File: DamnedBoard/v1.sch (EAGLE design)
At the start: 17 parts, among them U1 EFM32ZG108, U2 MAX44009EDT+T21-0490D-M

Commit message: OSH Parkifying layout.
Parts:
- removed R3: 0, SparkFun-Resistors:0OHM-0603-1/10W-5%
- added JP2, JP3: JUMPER-SMT_2_NC_TRACE_NO-SILK, SparkFun-Jumpers:JUMPER-SMT_2_NC_TRACE_NO-SILK
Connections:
- removed net N$1: G1.+, R3.2
- new net +L: G1.+$1, JP2.2
- new net +R: G1.+$2, JP3.2
- net VCC: now also JP2.1, JP3.1; no longer R3.1
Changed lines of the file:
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@@
 <parts>
 <part name="TC1" library="TagConnect" deviceset="TC2050-IDC" device=""/>
-<part name="G1" library="boneyard" deviceset="LINX_BAT_HLD_001" device="" package3d_urn="urn:adsk.eagle:package:291704/2"/>
 <part name="U2" library="boneyard" deviceset="MAX44009EDT+T" device="21-0490D-M" package3d_urn="urn:adsk.eagle:package:291621/2"/>
 <part name="U1" library="boneyard" deviceset="EFM32ZG108" device=""/>
@@
 <part name="R2" library="SparkFun-Resistors" library_urn="urn:adsk.eagle:library:532" deviceset="68OHM" device="-0603-1/10W-1%" package3d_urn="urn:adsk.eagle:package:39650/1"/>
 <part name="U$1" library="boneyard" deviceset="DAMNED" device=""/>
-<part name="R3" library="SparkFun-Resistors" library_urn="urn:adsk.eagle:library:532" deviceset="0OHM" device="-0603-1/10W-5%" package3d_urn="urn:adsk.eagle:package:39650/1" value="0"/>
 <part name="C1" library="SparkFun-Capacitors" library_urn="urn:adsk.eagle:library:510" deviceset="1.0UF" device="-0603-16V-10%" package3d_urn="urn:adsk.eagle:package:37414/1" value="1.0uF"/>
 <part name="JP1" library="SparkFun-Jumpers" library_urn="urn:adsk.eagle:library:528" deviceset="JUMPER-SMT_2_NC_TRACE" device="_NO-SILK" package3d_urn="urn:adsk.eagle:package:39286/1"/>
@@
 <part name="C5" library="SparkFun-Capacitors" library_urn="urn:adsk.eagle:library:510" deviceset="0.1UF" device="-0402-16V-10%" package3d_urn="urn:adsk.eagle:package:37413/1" value="0.1uF"/>
 <part name="C6" library="SparkFun-Capacitors" library_urn="urn:adsk.eagle:library:510" deviceset="10UF" device="-0603-6.3V-20%" package3d_urn="urn:adsk.eagle:package:37414/1" value="10uF"/>
+<part name="G1" library="boneyard" deviceset="LINX_BAT_HLD_001" device="" package3d_urn="urn:adsk.eagle:package:291704/2"/>
+<part name="JP2" library="SparkFun-Jumpers" library_urn="urn:adsk.eagle:library:528" deviceset="JUMPER-SMT_2_NC_TRACE" device="_NO-SILK" package3d_urn="urn:adsk.eagle:package:39286/1"/>
+<part name="JP3" library="SparkFun-Jumpers" library_urn="urn:adsk.eagle:library:528" deviceset="JUMPER-SMT_2_NC_TRACE" device="_NO-SILK" package3d_urn="urn:adsk.eagle:package:39286/1"/>
 </parts>
 <sheets>
@@
 <instances>
 <instance part="TC1" gate="A" x="-27.94" y="50.8" rot="R180"/>
-<instance part="G1" gate="G$1" x="43.18" y="27.94"/>
 <instance part="U2" gate="A" x="86.36" y="22.86"/>
 <instance part="U1" gate="G$1" x="55.88" y="55.88"/>
@@
 </instance>
 <instance part="U$1" gate="G$1" x="48.26" y="104.14"/>
-<instance part="R3" gate="G$1" x="27.94" y="27.94"/>
 <instance part="C1" gate="G$1" x="142.24" y="63.5"/>
 <instance part="JP1" gate="G$1" x="33.02" y="58.42" smashed="yes">
@@
 <instance part="C5" gate="G$1" x="17.78" y="71.12"/>
 <instance part="C6" gate="G$1" x="5.08" y="71.12"/>
+<instance part="G1" gate="G$1" x="50.8" y="12.7"/>
+<instance part="JP2" gate="G$1" x="35.56" y="15.24" smashed="yes">
+<attribute name="NAME" x="33.02" y="17.78" size="1.778" layer="95" font="vector"/>
+</instance>
+<instance part="JP3" gate="G$1" x="35.56" y="10.16" smashed="yes">
+<attribute name="NAME" x="33.02" y="5.08" size="1.778" layer="95" font="vector"/>
+</instance>
 </instances>
 <busses>
@@
 <net name="VSS" class="0">
 <segment>
-<pinref part="G1" gate="G$1" pin="-"/>
 <pinref part="U1" gate="G$1" pin="VSS"/>
-<wire x1="53.34" y1="27.94" x2="76.2" y2="27.94" width="0.1524" layer="91"/>
-<wire x1="76.2" y1="27.94" x2="76.2" y2="43.18" width="0.1524" layer="91"/>
+<wire x1="76.2" y1="20.32" x2="76.2" y2="43.18" width="0.1524" layer="91"/>
 <pinref part="U2" gate="A" pin="GND"/>
 <wire x1="88.9" y1="20.32" x2="76.2" y2="20.32" width="0.1524" layer="91"/>
-<wire x1="76.2" y1="20.32" x2="76.2" y2="27.94" width="0.1524" layer="91"/>
-<junction x="76.2" y="27.94"/>
 <pinref part="U2" gate="A" pin="A0"/>
 <wire x1="88.9" y1="17.78" x2="76.2" y2="17.78" width="0.1524" layer="91"/>
@@
 <junction x="76.2" y="20.32"/>
 <label x="70.358" y="28.702" size="1.778" layer="95"/>
+<pinref part="G1" gate="G$1" pin="-"/>
+<wire x1="60.96" y1="12.7" x2="76.2" y2="12.7" width="0.1524" layer="91"/>
+<wire x1="76.2" y1="12.7" x2="76.2" y2="17.78" width="0.1524" layer="91"/>
+<junction x="76.2" y="17.78"/>
 </segment>
 <segment>
@@
 </segment>
 <segment>
-<pinref part="R3" gate="G$1" pin="1"/>
-<wire x1="22.86" y1="27.94" x2="12.7" y2="27.94" width="0.1524" layer="91"/>
-<label x="13.716" y="28.194" size="1.778" layer="95"/>
-</segment>
-<segment>
 <pinref part="TC1" gate="A" pin="1"/>
 <wire x1="-35.56" y1="55.88" x2="-43.18" y2="55.88" width="0.1524" layer="91"/>
@@
 <pinref part="C3" gate="G$1" pin="2"/>
 </segment>
+<segment>
+<pinref part="JP2" gate="G$1" pin="1"/>
+<wire x1="30.48" y1="15.24" x2="22.86" y2="15.24" width="0.1524" layer="91"/>
+<wire x1="22.86" y1="15.24" x2="22.86" y2="12.7" width="0.1524" layer="91"/>
+<wire x1="22.86" y1="12.7" x2="15.24" y2="12.7" width="0.1524" layer="91"/>
+<pinref part="JP3" gate="G$1" pin="1"/>
+<wire x1="30.48" y1="10.16" x2="22.86" y2="10.16" width="0.1524" layer="91"/>
+<wire x1="22.86" y1="10.16" x2="22.86" y2="12.7" width="0.1524" layer="91"/>
+<junction x="22.86" y="12.7"/>
+<label x="15.748" y="13.462" size="1.778" layer="95"/>
+</segment>
 </net>
 <net name="PA0" class="0">
@@
 <pinref part="D2" gate="G$1" pin="C"/>
 <wire x1="-17.78" y1="99.06" x2="-17.78" y2="86.36" width="0.1524" layer="91"/>
-</segment>
-</net>
-<net name="N$1" class="0">
-<segment>
-<pinref part="G1" gate="G$1" pin="+"/>
-<pinref part="R3" gate="G$1" pin="2"/>
-<wire x1="43.18" y1="27.94" x2="33.02" y2="27.94" width="0.1524" layer="91"/>
 </segment>
 </net>
@@
 </segment>
 </net>
+<net name="+R" class="0">
+<segment>
+<pinref part="G1" gate="G$1" pin="+$2"/>
+<pinref part="JP3" gate="G$1" pin="2"/>
+<wire x1="48.26" y1="10.16" x2="40.64" y2="10.16" width="0.1524" layer="91"/>
+<label x="41.402" y="10.414" size="1.778" layer="95"/>
+</segment>
+</net>
+<net name="+L" class="0">
+<segment>
+<pinref part="G1" gate="G$1" pin="+$1"/>
+<pinref part="JP2" gate="G$1" pin="2"/>
+<wire x1="48.26" y1="15.24" x2="40.64" y2="15.24" width="0.1524" layer="91"/>
+<label x="41.656" y="16.002" size="1.778" layer="95"/>
+</segment>
+</net>

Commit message: Progress on layout.
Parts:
- removed C3, C4, C5: 0.1uF, SparkFun-Capacitors:0.1UF-0402-16V-10%
- C2, C6: device SparkFun-Capacitors:10UF-0603-6.3V-20% -> SparkFun-Capacitors:10UF-0805-10V-10%
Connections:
- net N$5 renamed DCP
- net SWCLK renamed SWCLRIP
- net VCC: no longer C3.2, C4.1, C5.1
- net VSS: no longer C3.1, C4.2, C5.2
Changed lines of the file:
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@@
 <part name="C1" library="SparkFun-Capacitors" library_urn="urn:adsk.eagle:library:510" deviceset="1.0UF" device="-0603-16V-10%" package3d_urn="urn:adsk.eagle:package:37414/1" value="1.0uF"/>
 <part name="JP1" library="SparkFun-Jumpers" library_urn="urn:adsk.eagle:library:528" deviceset="JUMPER-SMT_2_NC_TRACE" device="_NO-SILK" package3d_urn="urn:adsk.eagle:package:39286/1"/>
-<part name="C2" library="SparkFun-Capacitors" library_urn="urn:adsk.eagle:library:510" deviceset="10UF" device="-0603-6.3V-20%" package3d_urn="urn:adsk.eagle:package:37414/1" value="10uF"/>
-<part name="C3" library="SparkFun-Capacitors" library_urn="urn:adsk.eagle:library:510" deviceset="0.1UF" device="-0402-16V-10%" package3d_urn="urn:adsk.eagle:package:37413/1" value="0.1uF"/>
-<part name="C4" library="SparkFun-Capacitors" library_urn="urn:adsk.eagle:library:510" deviceset="0.1UF" device="-0402-16V-10%" package3d_urn="urn:adsk.eagle:package:37413/1" value="0.1uF"/>
-<part name="C5" library="SparkFun-Capacitors" library_urn="urn:adsk.eagle:library:510" deviceset="0.1UF" device="-0402-16V-10%" package3d_urn="urn:adsk.eagle:package:37413/1" value="0.1uF"/>
-<part name="C6" library="SparkFun-Capacitors" library_urn="urn:adsk.eagle:library:510" deviceset="10UF" device="-0603-6.3V-20%" package3d_urn="urn:adsk.eagle:package:37414/1" value="10uF"/>
+<part name="C2" library="SparkFun-Capacitors" library_urn="urn:adsk.eagle:library:510" deviceset="10UF" device="-0805-10V-10%" package3d_urn="urn:adsk.eagle:package:37429/1" value="10uF"/>
+<part name="C6" library="SparkFun-Capacitors" library_urn="urn:adsk.eagle:library:510" deviceset="10UF" device="-0805-10V-10%" package3d_urn="urn:adsk.eagle:package:37429/1" value="10uF"/>
 <part name="G1" library="boneyard" deviceset="LINX_BAT_HLD_001" device="" package3d_urn="urn:adsk.eagle:package:291704/2"/>
 <part name="JP2" library="SparkFun-Jumpers" library_urn="urn:adsk.eagle:library:528" deviceset="JUMPER-SMT_2_NC_TRACE" device="_NO-SILK" package3d_urn="urn:adsk.eagle:package:39286/1"/>
@@
 </instance>
 <instance part="C2" gate="G$1" x="129.54" y="83.82"/>
-<instance part="C3" gate="G$1" x="142.24" y="83.82"/>
-<instance part="C4" gate="G$1" x="137.16" y="50.8"/>
-<instance part="C5" gate="G$1" x="17.78" y="71.12"/>
 <instance part="C6" gate="G$1" x="5.08" y="71.12"/>
 <instance part="G1" gate="G$1" x="50.8" y="12.7"/>
@@
 </segment>
 <segment>
+<label x="-1.016" y="63.754" size="1.778" layer="95"/>
+<pinref part="C6" gate="G$1" pin="2"/>
+<wire x1="5.08" y1="68.58" x2="5.08" y2="63.5" width="0.1524" layer="91"/>
+</segment>
+<segment>
 <pinref part="C2" gate="G$1" pin="1"/>
 <wire x1="129.54" y1="88.9" x2="129.54" y2="93.98" width="0.1524" layer="91"/>
-<wire x1="129.54" y1="93.98" x2="142.24" y2="93.98" width="0.1524" layer="91"/>
-<wire x1="142.24" y1="93.98" x2="142.24" y2="88.9" width="0.1524" layer="91"/>
-<wire x1="142.24" y1="93.98" x2="142.24" y2="104.14" width="0.1524" layer="91"/>
-<junction x="142.24" y="93.98"/>
-<label x="143.256" y="102.108" size="1.778" layer="95"/>
-<pinref part="C3" gate="G$1" pin="1"/>
-</segment>
-<segment>
-<pinref part="C4" gate="G$1" pin="2"/>
-<wire x1="137.16" y1="48.26" x2="137.16" y2="40.64" width="0.1524" layer="91"/>
-<label x="138.176" y="41.402" size="1.778" layer="95"/>
-</segment>
-<segment>
-<pinref part="C5" gate="G$1" pin="2"/>
-<label x="6.604" y="61.214" size="1.778" layer="95"/>
-<pinref part="C6" gate="G$1" pin="2"/>
-<wire x1="5.08" y1="68.58" x2="5.08" y2="63.5" width="0.1524" layer="91"/>
-<wire x1="5.08" y1="63.5" x2="17.78" y2="63.5" width="0.1524" layer="91"/>
-<wire x1="17.78" y1="63.5" x2="17.78" y2="68.58" width="0.1524" layer="91"/>
+<label x="124.46" y="91.44" size="1.778" layer="95"/>
 </segment>
 </net>
@@
 <pinref part="U1" gate="G$1" pin="IOVDD_0"/>
 <label x="30.988" y="76.454" size="1.778" layer="95"/>
-<pinref part="C5" gate="G$1" pin="1"/>
-<wire x1="43.18" y1="76.2" x2="17.78" y2="76.2" width="0.1524" layer="91"/>
+<wire x1="43.18" y1="76.2" x2="5.08" y2="76.2" width="0.1524" layer="91"/>
 <pinref part="C6" gate="G$1" pin="1"/>
-<wire x1="17.78" y1="76.2" x2="5.08" y2="76.2" width="0.1524" layer="91"/>
-<junction x="17.78" y="76.2"/>
 <wire x1="5.08" y1="76.2" x2="5.08" y2="81.28" width="0.1524" layer="91"/>
 <junction x="5.08" y="76.2"/>
@@
 <pinref part="U1" gate="G$1" pin="IOVDD_5"/>
 <label x="119.634" y="56.388" size="1.778" layer="95"/>
-<pinref part="C4" gate="G$1" pin="1"/>
-<wire x1="111.76" y1="55.88" x2="137.16" y2="55.88" width="0.1524" layer="91"/>
+<wire x1="111.76" y1="55.88" x2="124.46" y2="55.88" width="0.1524" layer="91"/>
 </segment>
 <segment>
@@
 <wire x1="111.76" y1="73.66" x2="129.54" y2="73.66" width="0.1524" layer="91"/>
 <wire x1="129.54" y1="73.66" x2="142.24" y2="73.66" width="0.1524" layer="91"/>
-<wire x1="142.24" y1="73.66" x2="142.24" y2="81.28" width="0.1524" layer="91"/>
 <pinref part="C2" gate="G$1" pin="2"/>
 <wire x1="129.54" y1="81.28" x2="129.54" y2="73.66" width="0.1524" layer="91"/>
 <junction x="129.54" y="73.66"/>
 <label x="119.888" y="74.168" size="1.778" layer="95"/>
-<pinref part="C3" gate="G$1" pin="2"/>
 </segment>
 <segment>
@@
 </segment>
 </net>
-<net name="SWCLK" class="0">
+<net name="SWCLRIP" class="0">
 <segment>
 <pinref part="U1" gate="G$1" pin="PF0"/>
@@
 </segment>
 </net>
-<net name="N$5" class="0">
+<net name="DCP" class="0">
 <segment>
 <pinref part="U1" gate="G$1" pin="DECOUPLE"/>

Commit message: Candidate for manufacturing.
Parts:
- removed JP3: JUMPER-SMT_2_NC_TRACE_NO-SILK, SparkFun-Jumpers:JUMPER-SMT_2_NC_TRACE_NO-SILK
- removed TC1: TC2050-IDC, TagConnect:TC2050-IDC
- added J1: CORTEX_DEBUG_SMD, SparkFun-Connectors:CORTEX_DEBUG_SMD
- added TP1, TP2, TP3, TP4: TEST-POINT3, SparkFun-Connectors:TEST-POINT3
- U$1: value DAMNED -> COPYRIGHT; device boneyard:DAMNED -> boneyard:COPYRIGHT
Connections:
- net N$4 renamed AVDD
- removed net SWCLRIP: TC1.4, U1.PF0
- new net SWDCLK: J1.SWDCLK/TCK, U1.PF0
- net +R: no longer JP3.2
- net NRESET: now also J1.!RESET; no longer TC1.10
- net SCL: now also TP2.1; no longer TC1.8
- net SDA: now also TP1.1; no longer TC1.7
- net SWDIO: now also J1.SWDIO/TMS; no longer TC1.2
- net VCC: now also J1.VCC; no longer JP3.1, TC1.1
- net VSS: now also J1.GND@3, J1.GND@5, J1.GNDDTCT, TP3.1, TP4.1; no longer TC1.3, TC1.5, TC1.9

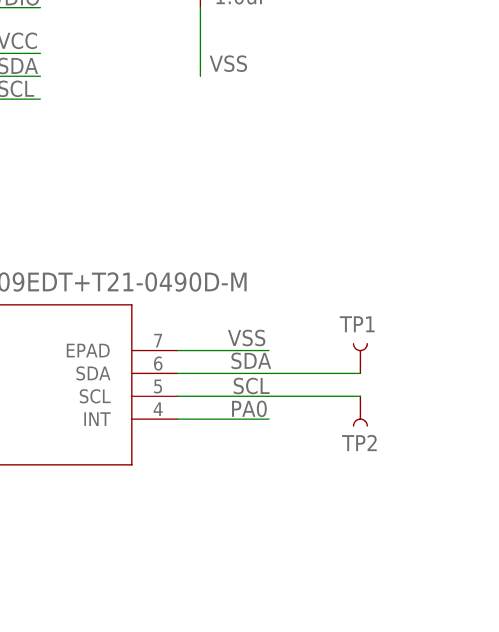
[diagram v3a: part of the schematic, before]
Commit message: Added pullups to i2c
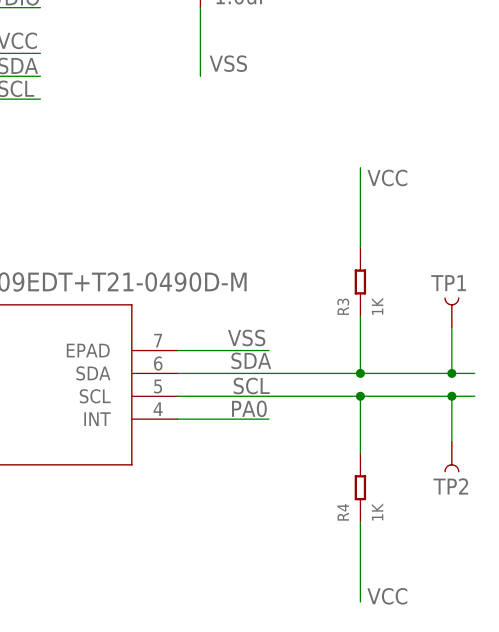
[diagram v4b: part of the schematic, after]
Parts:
- added R3, R4: 1K, Seeed-Resistor:SMD-RES-1K-5%-1/16W(0402)
- TP1, TP2: value TEST-POINT3 -> TEST-POINT3X5; device SparkFun-Connectors:TEST-POINT3 -> SparkFun-Connectors:TEST-POINT3X5
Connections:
- net SCL: now also R4.2
- net SDA: now also R3.1
- net VCC: now also R3.2, R4.1
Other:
- moved on the sheet: TP1, TP2
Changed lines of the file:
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@@
 <layer number="115" name="ReferenceISLANDS" color="7" fill="1" visible="yes" active="yes"/>
 <layer number="116" name="Patch_BOT" color="9" fill="4" visible="yes" active="yes"/>
+<layer number="117" name="BACKMAAT1" color="7" fill="1" visible="no" active="no"/>
 <layer number="118" name="Rect_Pads" color="7" fill="1" visible="yes" active="yes"/>
+<layer number="119" name="KAP_TEKEN" color="7" fill="1" visible="no" active="no"/>
+<layer number="120" name="KAP_MAAT1" color="7" fill="1" visible="no" active="no"/>
 <layer number="121" name="_tsilk" color="7" fill="1" visible="yes" active="yes"/>
 <layer number="122" name="_bsilk" color="7" fill="1" visible="yes" active="yes"/>
@@
 <layer number="128" name="_bValues" color="7" fill="1" visible="yes" active="yes"/>
 <layer number="129" name="Mask" color="7" fill="1" visible="yes" active="yes"/>
+<layer number="130" name="SMDSTROOK" color="7" fill="1" visible="no" active="no"/>
 <layer number="131" name="tAdjust" color="7" fill="1" visible="yes" active="yes"/>
 <layer number="132" name="bAdjust" color="7" fill="1" visible="yes" active="yes"/>
+<layer number="133" name="bottom_silk" color="7" fill="1" visible="no" active="no"/>
+<layer number="134" name="silk_top" color="7" fill="1" visible="no" active="no"/>
+<layer number="135" name="silk_bottom" color="7" fill="1" visible="no" active="no"/>
+<layer number="136" name="silktop" color="7" fill="1" visible="no" active="yes"/>
+<layer number="137" name="silkbottom" color="7" fill="1" visible="no" active="yes"/>
 <layer number="144" name="Drill_legend" color="7" fill="1" visible="yes" active="yes"/>
+<layer number="145" name="DrillLegend_01-16" color="7" fill="1" visible="no" active="yes"/>
+<layer number="146" name="DrillLegend_01-20" color="7" fill="1" visible="no" active="yes"/>
 <layer number="150" name="Notes" color="7" fill="1" visible="yes" active="yes"/>
 <layer number="151" name="HeatSink" color="7" fill="1" visible="yes" active="yes"/>
@@
 <layer number="154" name="FabDoc2" color="7" fill="1" visible="yes" active="yes"/>
 <layer number="155" name="FabDoc3" color="7" fill="1" visible="yes" active="yes"/>
+<layer number="166" name="AntennaArea" color="7" fill="1" visible="yes" active="yes"/>
+<layer number="168" name="4mmHeightArea" color="7" fill="1" visible="yes" active="yes"/>
 <layer number="199" name="Contour" color="7" fill="1" visible="yes" active="yes"/>
 <layer number="200" name="200bmp" color="1" fill="10" visible="no" active="no"/>
@@
 <part name="U$1" library="boneyard" deviceset="COPYRIGHT" device=""/>
 <part name="J1" library="SparkFun-Connectors" library_urn="urn:adsk.eagle:library:513" deviceset="CORTEX_DEBUG" device="_SMD" package3d_urn="urn:adsk.eagle:package:38289/1"/>
-<part name="TP1" library="SparkFun-Connectors" library_urn="urn:adsk.eagle:library:513" deviceset="TEST-POINT" device="3" package3d_urn="urn:adsk.eagle:package:38286/1"/>
-<part name="TP2" library="SparkFun-Connectors" library_urn="urn:adsk.eagle:library:513" deviceset="TEST-POINT" device="3" package3d_urn="urn:adsk.eagle:package:38286/1"/>
 <part name="TP3" library="SparkFun-Connectors" library_urn="urn:adsk.eagle:library:513" deviceset="TEST-POINT" device="3" package3d_urn="urn:adsk.eagle:package:38286/1"/>
 <part name="TP4" library="SparkFun-Connectors" library_urn="urn:adsk.eagle:library:513" deviceset="TEST-POINT" device="3" package3d_urn="urn:adsk.eagle:package:38286/1"/>
+<part name="R3" library="Seeed-Resistor" library_urn="urn:adsk.eagle:library:474" deviceset="SMD-RES-1K-5%-1/16W(0402)" device="" package3d_urn="urn:adsk.eagle:package:32792/1" value="1K"/>
+<part name="R4" library="Seeed-Resistor" library_urn="urn:adsk.eagle:library:474" deviceset="SMD-RES-1K-5%-1/16W(0402)" device="" package3d_urn="urn:adsk.eagle:package:32792/1" value="1K"/>
+<part name="TP1" library="SparkFun-Connectors" library_urn="urn:adsk.eagle:library:513" deviceset="TEST-POINT" device="3X5" package3d_urn="urn:adsk.eagle:package:38285/1"/>
+<part name="TP2" library="SparkFun-Connectors" library_urn="urn:adsk.eagle:library:513" deviceset="TEST-POINT" device="3X5" package3d_urn="urn:adsk.eagle:package:38285/1"/>
 </parts>
 <sheets>
@@
 <instance part="U$1" gate="G$1" x="48.26" y="101.6"/>
 <instance part="J1" gate="G$1" x="-25.4" y="33.02"/>
-<instance part="TP1" gate="G$1" x="160.02" y="20.32" smashed="yes" rot="R90">
-<attribute name="NAME" x="161.798" y="26.67" size="1.778" layer="95" font="vector" rot="R180"/>
-</instance>
-<instance part="TP2" gate="G$1" x="160.02" y="17.78" smashed="yes" rot="R270">
-<attribute name="NAME" x="157.988" y="11.684" size="1.778" layer="95" font="vector"/>
-</instance>
 <instance part="TP3" gate="G$1" x="68.58" y="38.1" smashed="yes" rot="R180">
 <attribute name="NAME" x="59.436" y="37.338" size="1.778" layer="95" font="vector"/>
@@
 <instance part="TP4" gate="G$1" x="83.82" y="38.1" smashed="yes">
 <attribute name="NAME" x="92.964" y="38.862" size="1.778" layer="95" font="vector" rot="R180"/>
+</instance>
+<instance part="R3" gate="G$1" x="160.02" y="30.48" rot="R90"/>
+<instance part="R4" gate="G$1" x="160.02" y="7.62" rot="R90"/>
+<instance part="TP1" gate="G$1" x="170.18" y="25.4" smashed="yes" rot="R90">
+<attribute name="NAME" x="171.958" y="31.242" size="1.778" layer="95" font="vector" rot="R180"/>
+</instance>
+<instance part="TP2" gate="G$1" x="170.18" y="12.7" smashed="yes" rot="R270">
+<attribute name="NAME" x="168.148" y="6.858" size="1.778" layer="95" font="vector"/>
 </instance>
 </instances>
@@
 <pinref part="U2" gate="A" pin="SDA"/>
 <label x="145.542" y="20.828" size="1.778" layer="95"/>
+<wire x1="139.7" y1="20.32" x2="160.02" y2="20.32" width="0.1524" layer="91"/>
+<pinref part="R3" gate="G$1" pin="1"/>
+<wire x1="160.02" y1="20.32" x2="170.18" y2="20.32" width="0.1524" layer="91"/>
+<wire x1="170.18" y1="20.32" x2="172.72" y2="20.32" width="0.1524" layer="91"/>
+<wire x1="160.02" y1="26.67" x2="160.02" y2="20.32" width="0.1524" layer="91"/>
+<junction x="160.02" y="20.32"/>
 <pinref part="TP1" gate="G$1" pin="1"/>
-<wire x1="139.7" y1="20.32" x2="160.02" y2="20.32" width="0.1524" layer="91"/>
+<wire x1="170.18" y1="25.4" x2="170.18" y2="20.32" width="0.1524" layer="91"/>
+<junction x="170.18" y="20.32"/>
 </segment>
 </net>
@@
 <pinref part="U2" gate="A" pin="SCL"/>
 <label x="145.796" y="18.034" size="1.778" layer="95"/>
+<wire x1="139.7" y1="17.78" x2="160.02" y2="17.78" width="0.1524" layer="91"/>
+<pinref part="R4" gate="G$1" pin="2"/>
+<wire x1="160.02" y1="17.78" x2="170.18" y2="17.78" width="0.1524" layer="91"/>
+<wire x1="170.18" y1="17.78" x2="172.72" y2="17.78" width="0.1524" layer="91"/>
+<wire x1="160.02" y1="11.43" x2="160.02" y2="17.78" width="0.1524" layer="91"/>
+<junction x="160.02" y="17.78"/>
 <pinref part="TP2" gate="G$1" pin="1"/>
-<wire x1="139.7" y1="17.78" x2="160.02" y2="17.78" width="0.1524" layer="91"/>
+<wire x1="170.18" y1="12.7" x2="170.18" y2="17.78" width="0.1524" layer="91"/>
+<junction x="170.18" y="17.78"/>
 </segment>
 </net>
@@
 <label x="-18.288" y="123.19" size="1.778" layer="95" rot="R90"/>
 </segment>
-</net>
+<segment>
+<pinref part="R3" gate="G$1" pin="2"/>
+<wire x1="160.02" y1="34.29" x2="160.02" y2="43.18" width="0.1524" layer="91"/>
+<label x="160.782" y="41.148" size="1.778" layer="95"/>
+</segment>
+<segment>
+<pinref part="R4" gate="G$1" pin="1"/>
+<wire x1="160.02" y1="3.81" x2="160.02" y2="-5.08" width="0.1524" layer="91"/>
+<label x="160.782" y="-5.334" size="1.778" layer="95"/>
+</segment>
+</net>
